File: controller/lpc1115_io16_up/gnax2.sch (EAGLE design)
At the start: 76 parts, among them J2 CON_10-1.27THT, SW1 SWITCH_X, T1 BC547C, T2 BC807-40, U1 DMHC4035LSD, U2 SN74AUP1T32, U3 BD9G101G, U4 LPC1115FBD48/303, U5 M25P10, X1 12MHz, X3 FIDUCIAL_0.6-1.2MM, X8 FIDUCIAL_0.6-1.2MM, X9 FIDUCIAL_0.6-1.2MM

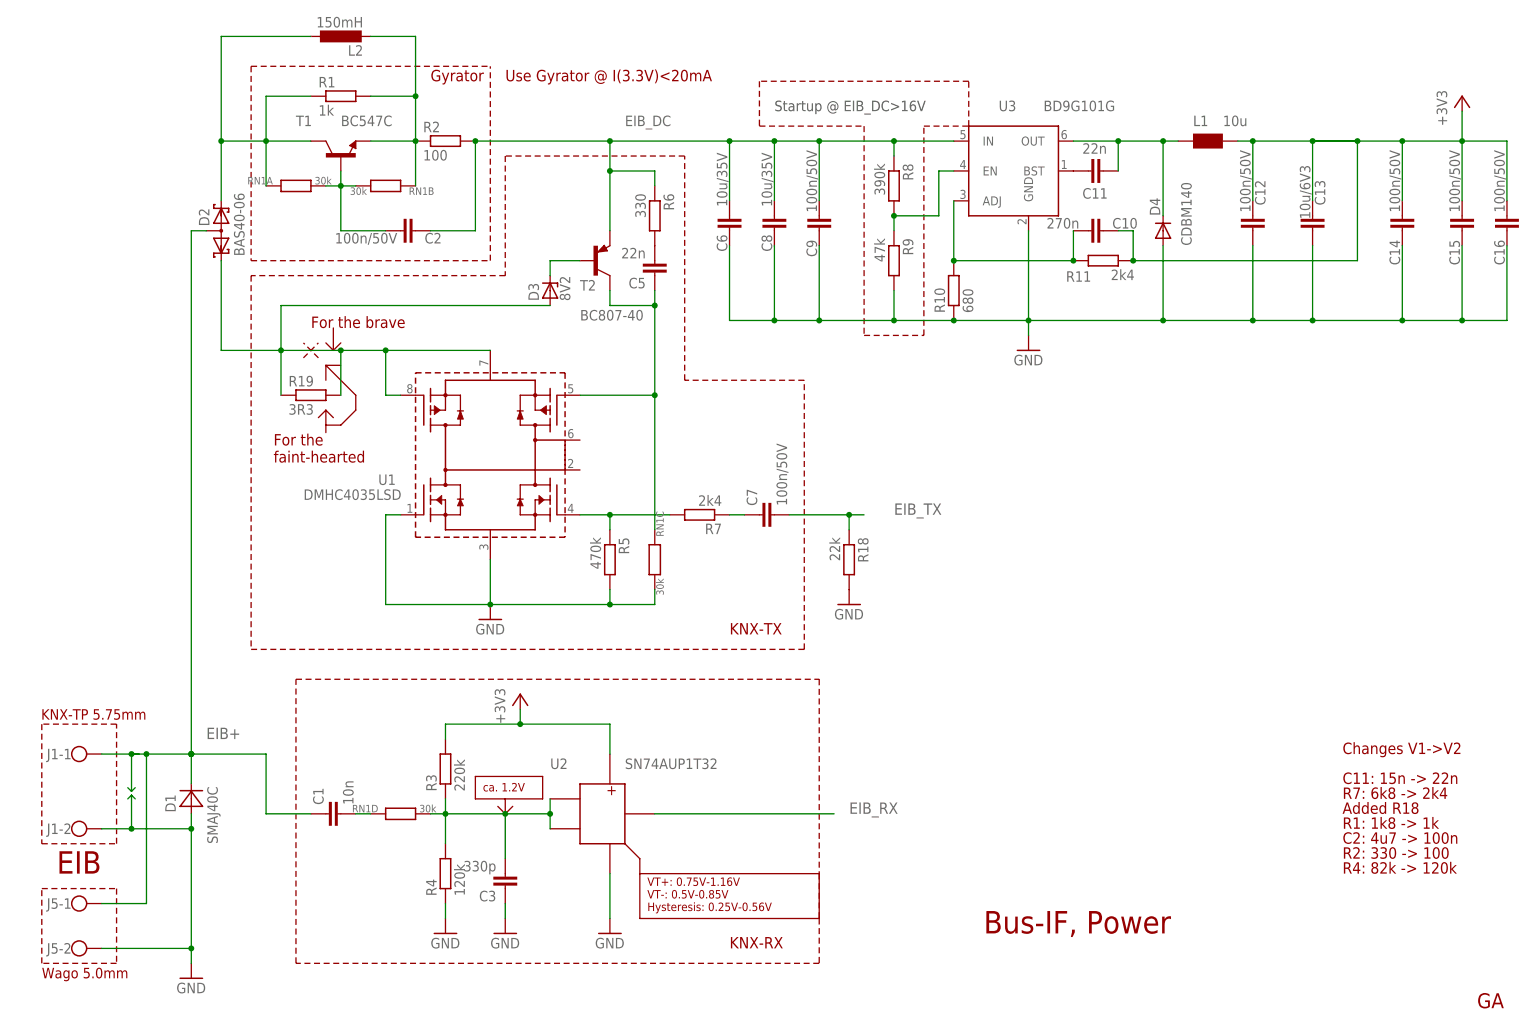
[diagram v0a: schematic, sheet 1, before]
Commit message: current limiter for transmitter, change prog led behaviour, fix clamp layout
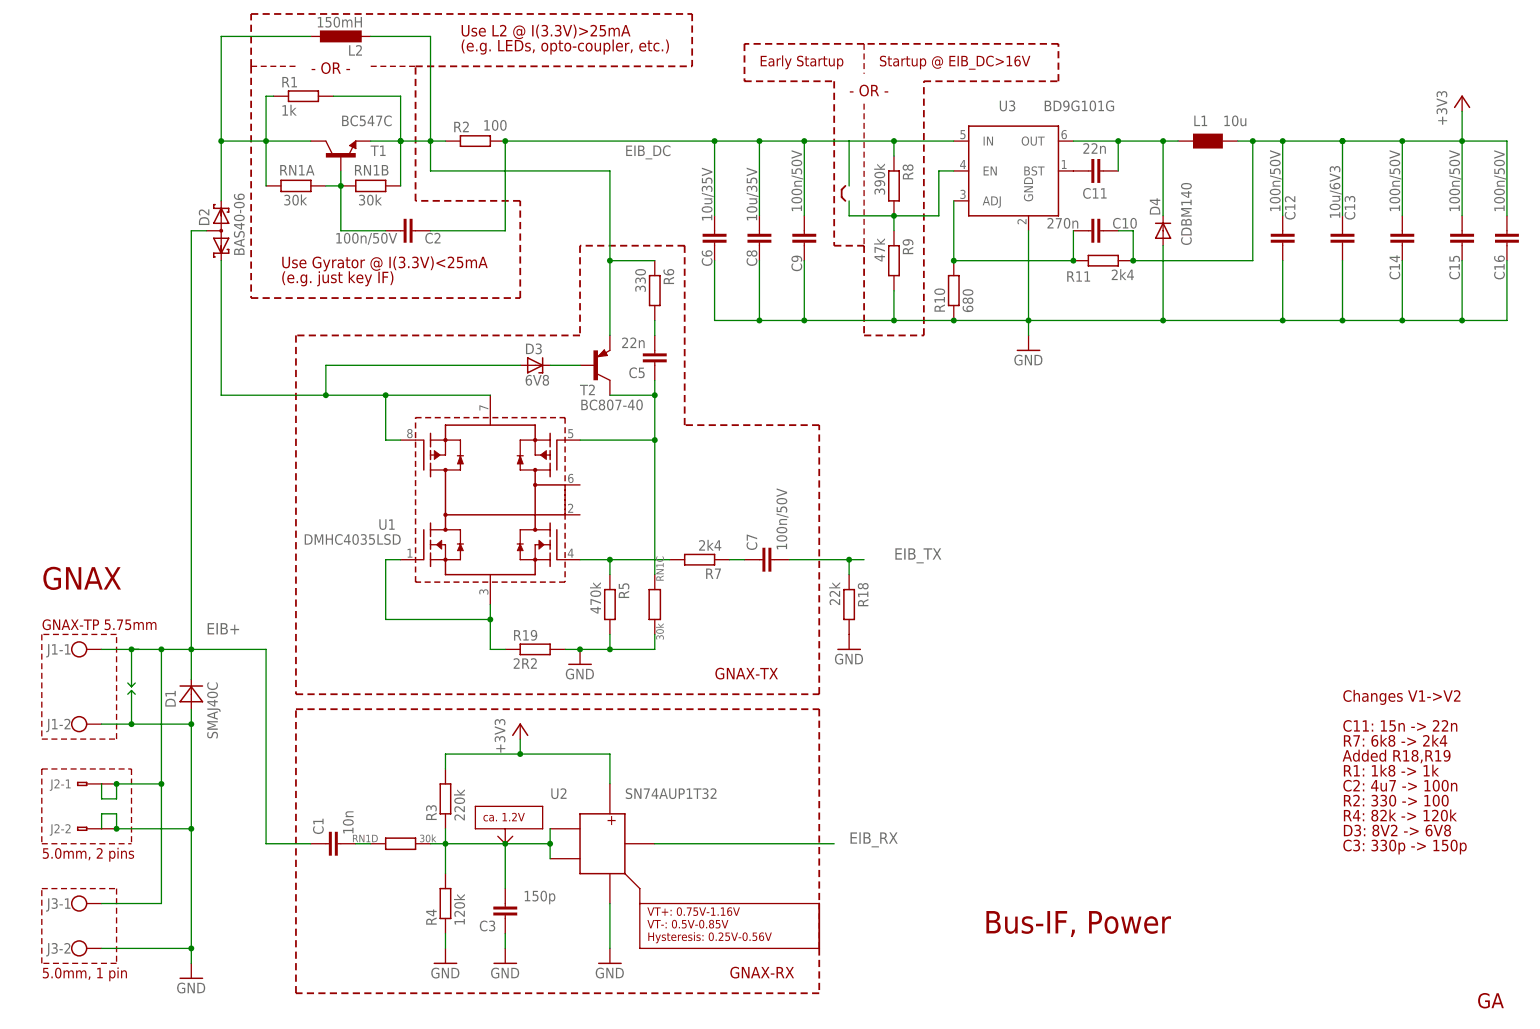
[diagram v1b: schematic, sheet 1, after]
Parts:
- removed J2: CON_10-1.27THT, 000_ga:CON_10-1.27THT
- removed SV1, SV2: (no value), con-lstb:MA05-1
- added J2-1, J2-2: 236-740-5,08, con-wago:236-740-5,08
- added J7: (no value), con-lstb:MA05-2
- added J8, J9: (no value), con-lstb:MA05-1
- C3: value 330p -> 150p
- D3: value 8V2 -> 6V8
- J3: device con-lstb:MA13-2 -> 000_ga:CON_2
- J4: value (none) -> CON_10-1.27THT; device con-lstb:MA05-2 -> 000_ga:CON_10-1.27THT
- J5: device 000_ga:CON_2 -> con-lstb:MA13-2
- R19: value 3R3 -> 2R2
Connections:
- removed net N$40: LED3.C, R17.2, SW1.S, SW1.S1
- new net FX: R19.1, U1.N1G, U1.N1S/N2S
- new net N$46: L2.2, R1.2, R2.1, R6.1, RN1B.P$1, T1.E, T2.E
- net EIB+: now also J2-1.A1, J2-1.B1, J3-1.KL, J5.1; no longer J3.1, J5-1.KL
- net EIB_DC: now also J5.6; no longer J3.6, R6.1, T2.E
- net GND: now also J2-2.B1, J3-2.KL, J5.2, J5.21, J7.2, J7.4, J7.6, J7.8, J7.9, J8.5, J9.5, R19.2, SW1.S, SW1.S1; no longer J2.9, J3.2, J3.21, J4.2, J4.4, J4.6, J4.8, J5-2.KL, R17.1, SV1.5, SV2.5, U1.N1G, U1.N1S/N2S
- net N$1: no longer R19.1, R19.2
- net N$10: now also J6.5; no longer J4.5
- net N$11: now also J6.3; no longer J4.3
- net N$13: now also J6.1; no longer J4.1
- net N$16: now also J7.5; no longer J6.5
- net N$17: now also J7.3; no longer J6.3
- net N$22: now also J7.7; no longer J6.7
- net N$23: now also J7.1; no longer J6.1
- net N$25: now also LED3.C, R17.2; no longer L2.2, R1.2, R2.1, RN1B.P$1, T1.E
- net N$29: now also J8.3; no longer SV1.3
- net N$30: now also J8.2; no longer SV1.2
- net N$31: now also J8.4; no longer SV1.4
- net N$32: now also J9.1; no longer SV2.1
- net N$33: now also J9.2; no longer SV2.2
- net N$34: now also J9.3; no longer SV2.3
- net N$35: now also J9.4; no longer SV2.4
- net N$36: now also J8.1; no longer SV1.1
- net N$38: now also J5.3; no longer J3.3
- net N$41: now also J5.7; no longer J3.7
- net N$42: now also J5.9; no longer J3.9
- net N$43: now also J5.11; no longer J3.11
- net N$44: now also J5.13; no longer J3.13
- net N$45: now also J5.4; no longer J3.4
- net N$47: now also J5.8; no longer J3.8
- net N$48: now also J5.10; no longer J3.10
- net N$49: now also J5.12; no longer J3.12
- net N$5: now also J6.7; no longer J4.7
- net N$50: now also J5.14; no longer J3.14
- net N$58: now also J5.15; no longer J3.15
- net N$59: now also J5.17; no longer J3.17
- net N$60: now also J5.16; no longer J3.16
- net N$61: now also J5.18; no longer J3.18
- net N$63: now also J5.19; no longer J3.19
- net N$64: now also J5.20; no longer J3.20
- net N$65: now also J5.22; no longer J3.22
- net N$66: now also J5.23; no longer J3.23
- net N$67: now also J5.24; no longer J3.24
- net N$68: now also J5.25; no longer J3.25
- net N$69: now also J5.26; no longer J3.26
- net RESET: now also J4.10; no longer J2.10
- net SWCLK: now also J4.4; no longer J2.4
- net SWDIO: now also J4.2; no longer J2.2
- net VCC: now also J4.1, J5.5, J7.10, LED3.A; no longer J2.1, J3.5, J4.10
- net XIO23: now also R17.1; no longer LED3.A
- net XIO8/ISP_EN: now also J4.7; no longer J2.7
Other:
- note added: "(e.g. LEDs, opto-coupler, etc.)"
- note added: "(e.g. just key IF)"
- note added: "- OR -"
- note added: "5.0mm, 1 pin"
- note added: "5.0mm, 2 pins"
- note added: "Added R18,R19"
- note added: "C3: 330p -> 150p"
- note added: "D3: 8V2 -> 6V8"
- note added: "Early Startup"
- note added: "GNAX"
- note added: "GNAX-RX"
- note added: "GNAX-TP 5.75mm"
- note added: "GNAX-TX"
- note added: "J8/J9 combined in 2*5"
- note added: "Moved LED3 to VCC"
- note added: "PROG-SWITCH"
- note added: "Use Gyrator @ I(3.3V)<25mA"
- note added: "Use L2 @ I(3.3V)>25mA"
- note removed: "Added R18"
- note removed: "EIB"
- note removed: "For the brave"
- note removed: "For the faint-hearted"
- note removed: "Gyrator"
- note removed: "KNX-RX"
- note removed: "KNX-TP 5.75mm"
- note removed: "KNX-TX"
- note removed: "Use Gyrator @ I(3.3V)<20mA"
- note removed: "Wago 5.0mm"
- moved on the sheet: C1, C12, C13, C14, C15, C16, C3, C5, C6, C7, C8, C9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

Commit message: fix receiver voltage protection
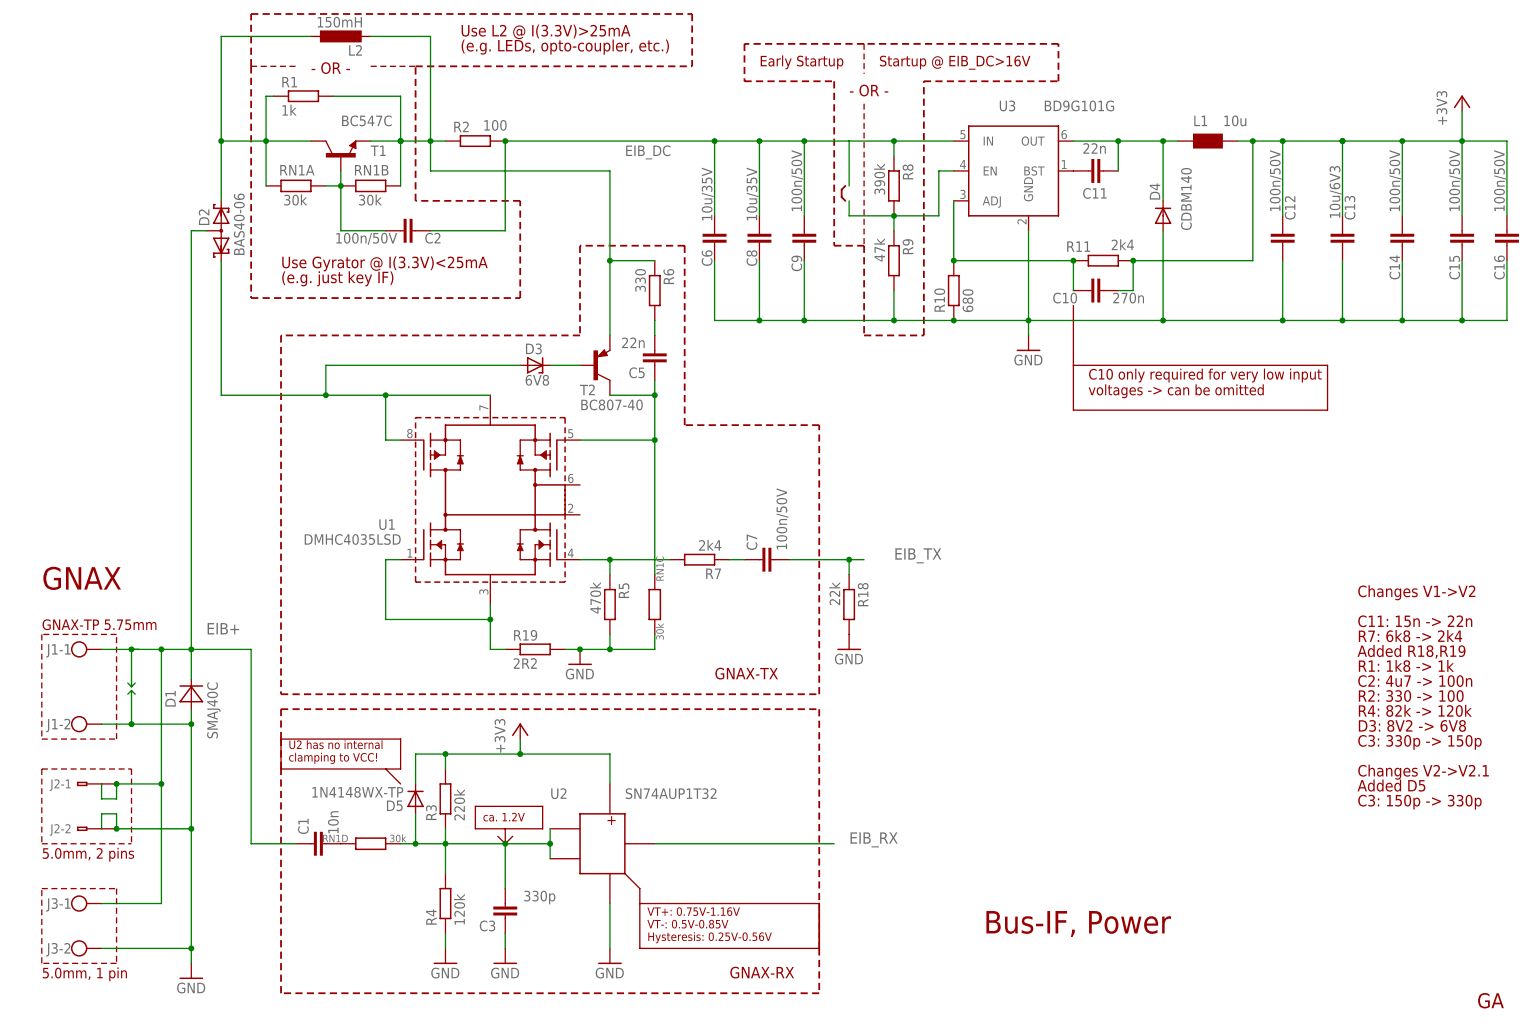
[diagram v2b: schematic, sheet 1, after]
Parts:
- added D5: 1N4148WX-TP, diode:DIODE-SOD323-R
- C3: value 150p -> 330p
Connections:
- net N$14: now also D5.A
- net VCC: now also D5.C
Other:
- note added: "Added D5"
- note added: "Application connector !!! some pins shared with J8/J9 !!!"
- note added: "C10 only required for very low input voltages -> can be omitted"
- note added: "C3: 150p -> 330p"
- note added: "Changes V2->V2.1"
- note added: "Pull to GND to stay in safe bootloader if ISP fails"
- note added: "U2 has no internal clamping to VCC!"
- note added: "Values of RN2/3/4/5/6 depend on application"
- note added: "XIO23 also PROG key!"
- moved on the sheet: C1, C10, D4, RN1D
